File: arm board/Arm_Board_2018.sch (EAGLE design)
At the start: 190 parts, among them J1 RJ45KEYSTONE-942, J10 APP_2POS_CONFIGGENERAL_CONFIG, J11 APP_2POS_CONFIGGENERAL_CONFIG, J12 APP_2POS_CONFIGGENERAL_CONFIG, J13 APP_2POS_CONFIGGENERAL_CONFIG, J14 SL02, J15 SL02, J16 SL02, J2 JTAG_ARM_10PIN, J4 SL02, J5 APP_2POS_CONFIGGENERAL_CONFIG, J6 APP_2POS_CONFIGGENERAL_CONFIG, J7 APP_2POS_CONFIGGENERAL_CONFIG, J9 APP_2POS_CONFIGGENERAL_CONFIG, Q1 Q_IRF7437SMD, U1 TM4C1294NCPDT, U2 HX1198FNL, U3 SLVU2.8-4, Y1 NX3225GA, Y2 CRYATL_32K_SMD

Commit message: Switched wires to nets, corrected couple of naming errors
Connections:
- removed net MOTOR23_CURRENT_SENSOR: U$21.VOUT
- removed net N$52: C44.1, C45.1, C46.1, C47.1
- removed net N$82: R61.1, R62.1, R63.1, R64.1, R65.1, R66.1
- removed net N$85: R55.2
- removed net N$86: R54.2
- net GND: now also C44.1, C45.1, C46.1, C47.1, R54.2, R55.2, R61.1, R62.1, R63.1, R64.1, R65.1, R66.1
- net MOTOR3_CURRENT_SENSOR: now also U$21.VOUT
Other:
- note added: "MAIN POWER INPUT"
- note added: "MOTOR MANUAL CONTROL LEDS"
- note removed: "BOARD LEDS"
- note removed: "MAIN POWER LINE"
- moved on the sheet: C21, C23, C25, C26, C29, C30, C33, C34, C37, C38, C41, C42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

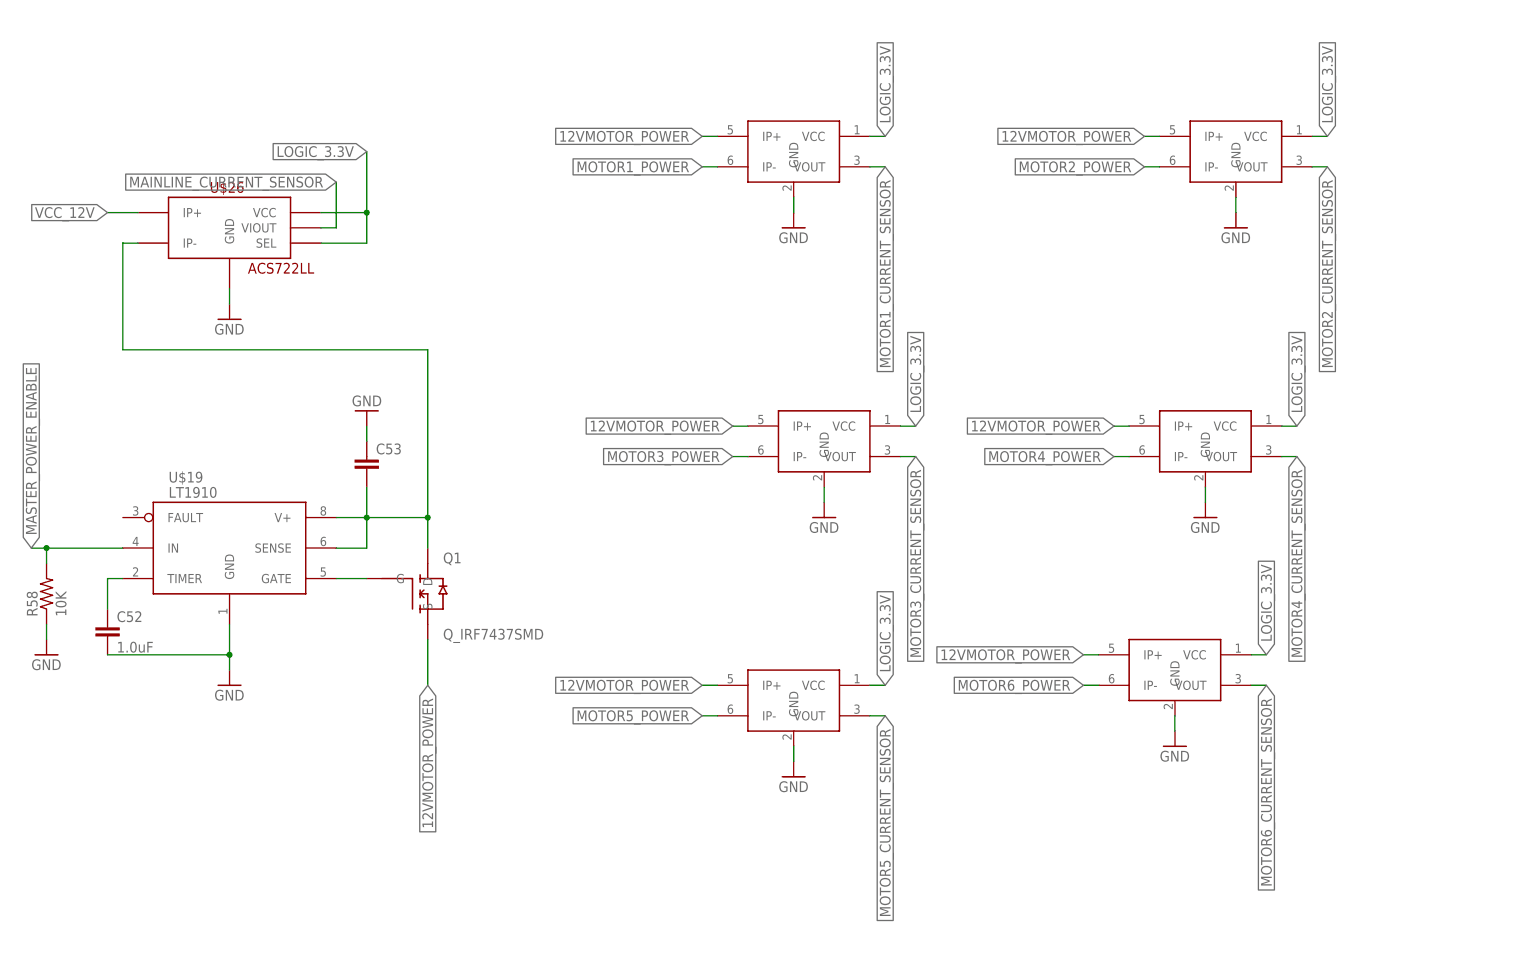
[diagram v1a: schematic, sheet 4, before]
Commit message: Fixed remaining SCH issues, warnings, and missing parts
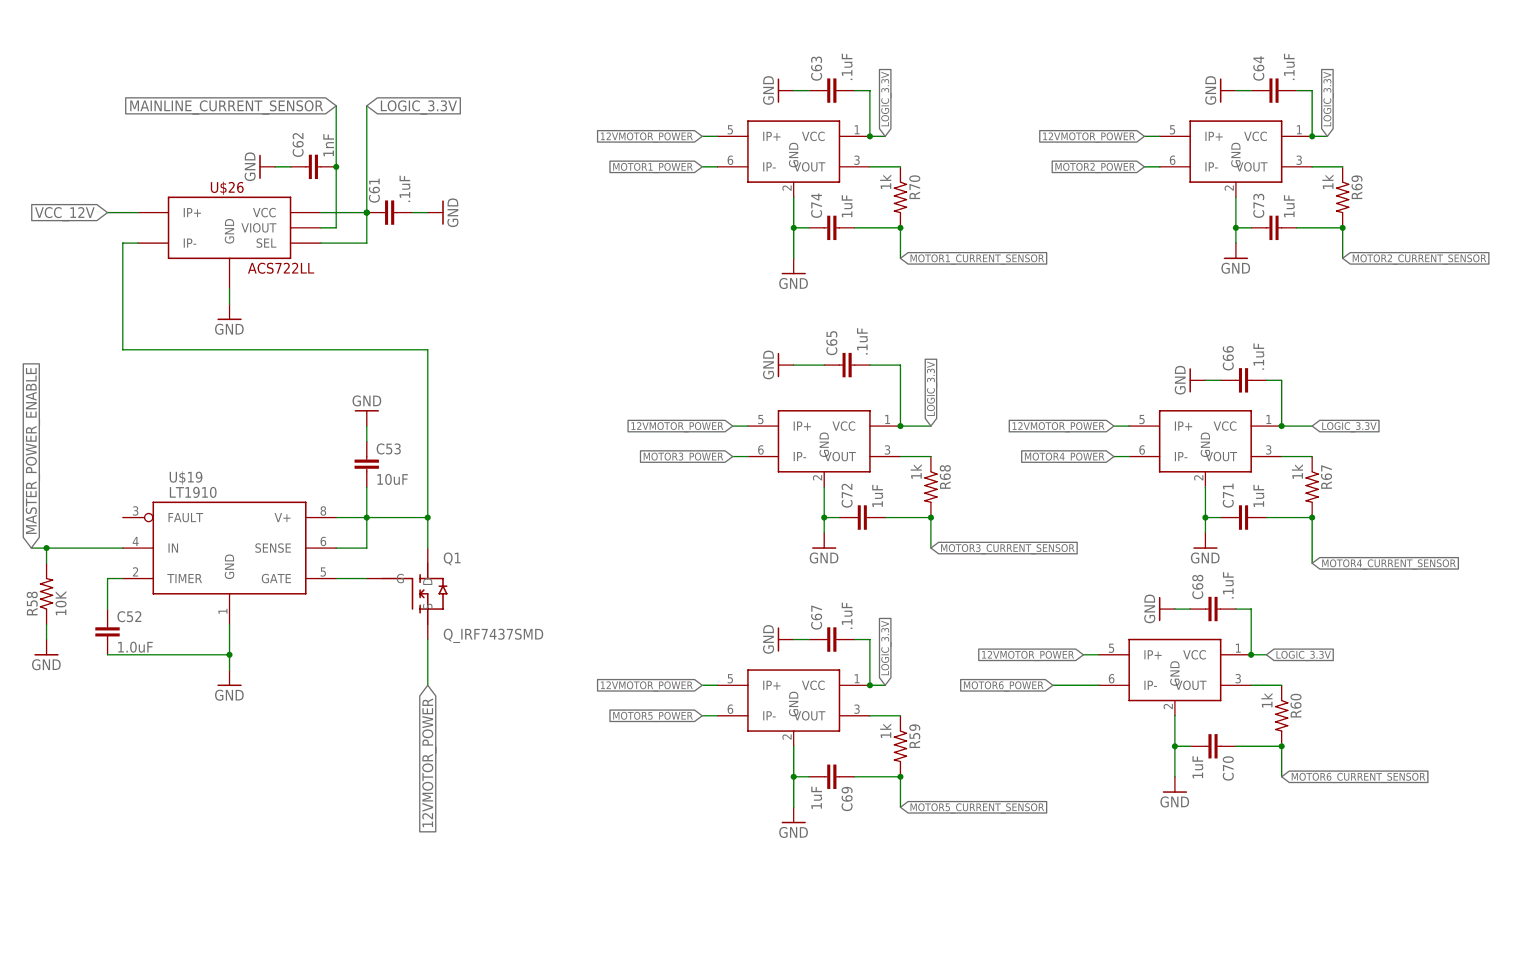
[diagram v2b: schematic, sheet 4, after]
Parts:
- removed C50: 2.2uF, SparkFun-Passives:CAP0603-CAP
- added C61, C63, C64, C65, C66, C67, C68: .1uF, SparkFun-Passives:CAP0603-CAP
- added C62: 1nF, SparkFun-Passives:CAP0603-CAP
- added C69, C70, C71, C72, C73, C74: 1uF, SparkFun-Passives:CAP0603-CAP
- added C75: 2.2uF, SparkFun-Capacitors:CAP1206
- added R59, R60, R67, R68, R69, R70: 1k, SparkFun-Passives:RESISTOR0402-RES
- C48, C49, C54: value (none) -> .1uF
- C51: device SparkFun-Passives:CAP0603-CAP -> SparkFun-Capacitors:CAP1206
- C53: value (none) -> 10uF
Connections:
- new net N$12: R59.1, U$24.VOUT
- new net N$13: R60.1, U$25.VOUT
- new net N$20: R67.1, U$23.VOUT
- new net N$32: R68.1, U$21.VOUT
- new net N$38: R69.1, U$22.VOUT
- new net N$44: R70.1, U$20.VOUT
- net GND: now also C51.1, C61.2, C62.1, C63.1, C64.1, C65.1, C66.1, C67.1, C68.1, C69.2, C70.2, C71.1, C72.1, C73.1, C74.1, C75.2; no longer C50.2, C51.2
- net LOGIC_3.3V: now also C61.1, C63.2, C64.2, C65.2, C66.2, C67.2, C68.2, C75.1; no longer C50.1
- net MAINLINE_CURRENT_SENSOR: now also C62.2
- net MOTOR1_CURRENT_SENSOR: now also C74.2, R70.2; no longer U$20.VOUT
- net MOTOR2_CURRENT_SENSOR: now also C73.2, R69.2; no longer U$22.VOUT
- net MOTOR3_CURRENT_SENSOR: now also C72.2, R68.2; no longer U$21.VOUT
- net MOTOR4_CURRENT_SENSOR: now also C71.2, R67.2; no longer U$23.VOUT
- net MOTOR5_CURRENT_SENSOR: now also C69.1, R59.2; no longer U$24.VOUT
- net MOTOR6_CURRENT_SENSOR: now also C70.1, R60.2; no longer U$25.VOUT
- net VCC_12V: now also C51.2; no longer C51.1
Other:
- moved on the sheet: C51

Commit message: Changed +3V3 to LOGIC_3.3V
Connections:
- removed net +3V3: C1.1, C10.1, C11.1, C2.1, C3.1, C4.1, C8.1, C9.1, J2.VTARGET, LED3.A, R1.1, R12.2, R13.2, R17.1, R2.1, R3.1, R4.1, U1G$2.VDD@101, U1G$2.VDD@113, U1G$2.VDD@122, U1G$2.VDD@16, U1G$2.VDD@26, U1G$2.VDD@28, U1G$2.VDD@39, U1G$2.VDD@47, U1G$2.VDD@51, U1G$2.VDD@52, U1G$2.VDD@69, U1G$2.VDD@7, U1G$2.VDD@79, U1G$2.VDD@90, U1G$2.VDDA@8, U1G$2.VREFA+@9, U2.P$2, U2.P$7
- net LOGIC_3.3V: now also C1.1, C10.1, C11.1, C2.1, C3.1, C4.1, C8.1, C9.1, J2.VTARGET, LED3.A, R1.1, R12.2, R13.2, R17.1, R2.1, R3.1, R4.1, U1G$2.VDD@101, U1G$2.VDD@113, U1G$2.VDD@122, U1G$2.VDD@16, U1G$2.VDD@26, U1G$2.VDD@28, U1G$2.VDD@39, U1G$2.VDD@47, U1G$2.VDD@51, U1G$2.VDD@52, U1G$2.VDD@69, U1G$2.VDD@7, U1G$2.VDD@79, U1G$2.VDD@90, U1G$2.VDDA@8, U1G$2.VREFA+@9, U2.P$2, U2.P$7
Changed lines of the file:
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@@
 </segment>
 </net>
-<net name="+3V3" class="0">
+<net name="LOGIC_3.3V" class="0">
 <segment>
 <pinref part="+3V1" gate="G$1" pin="+3V3"/>

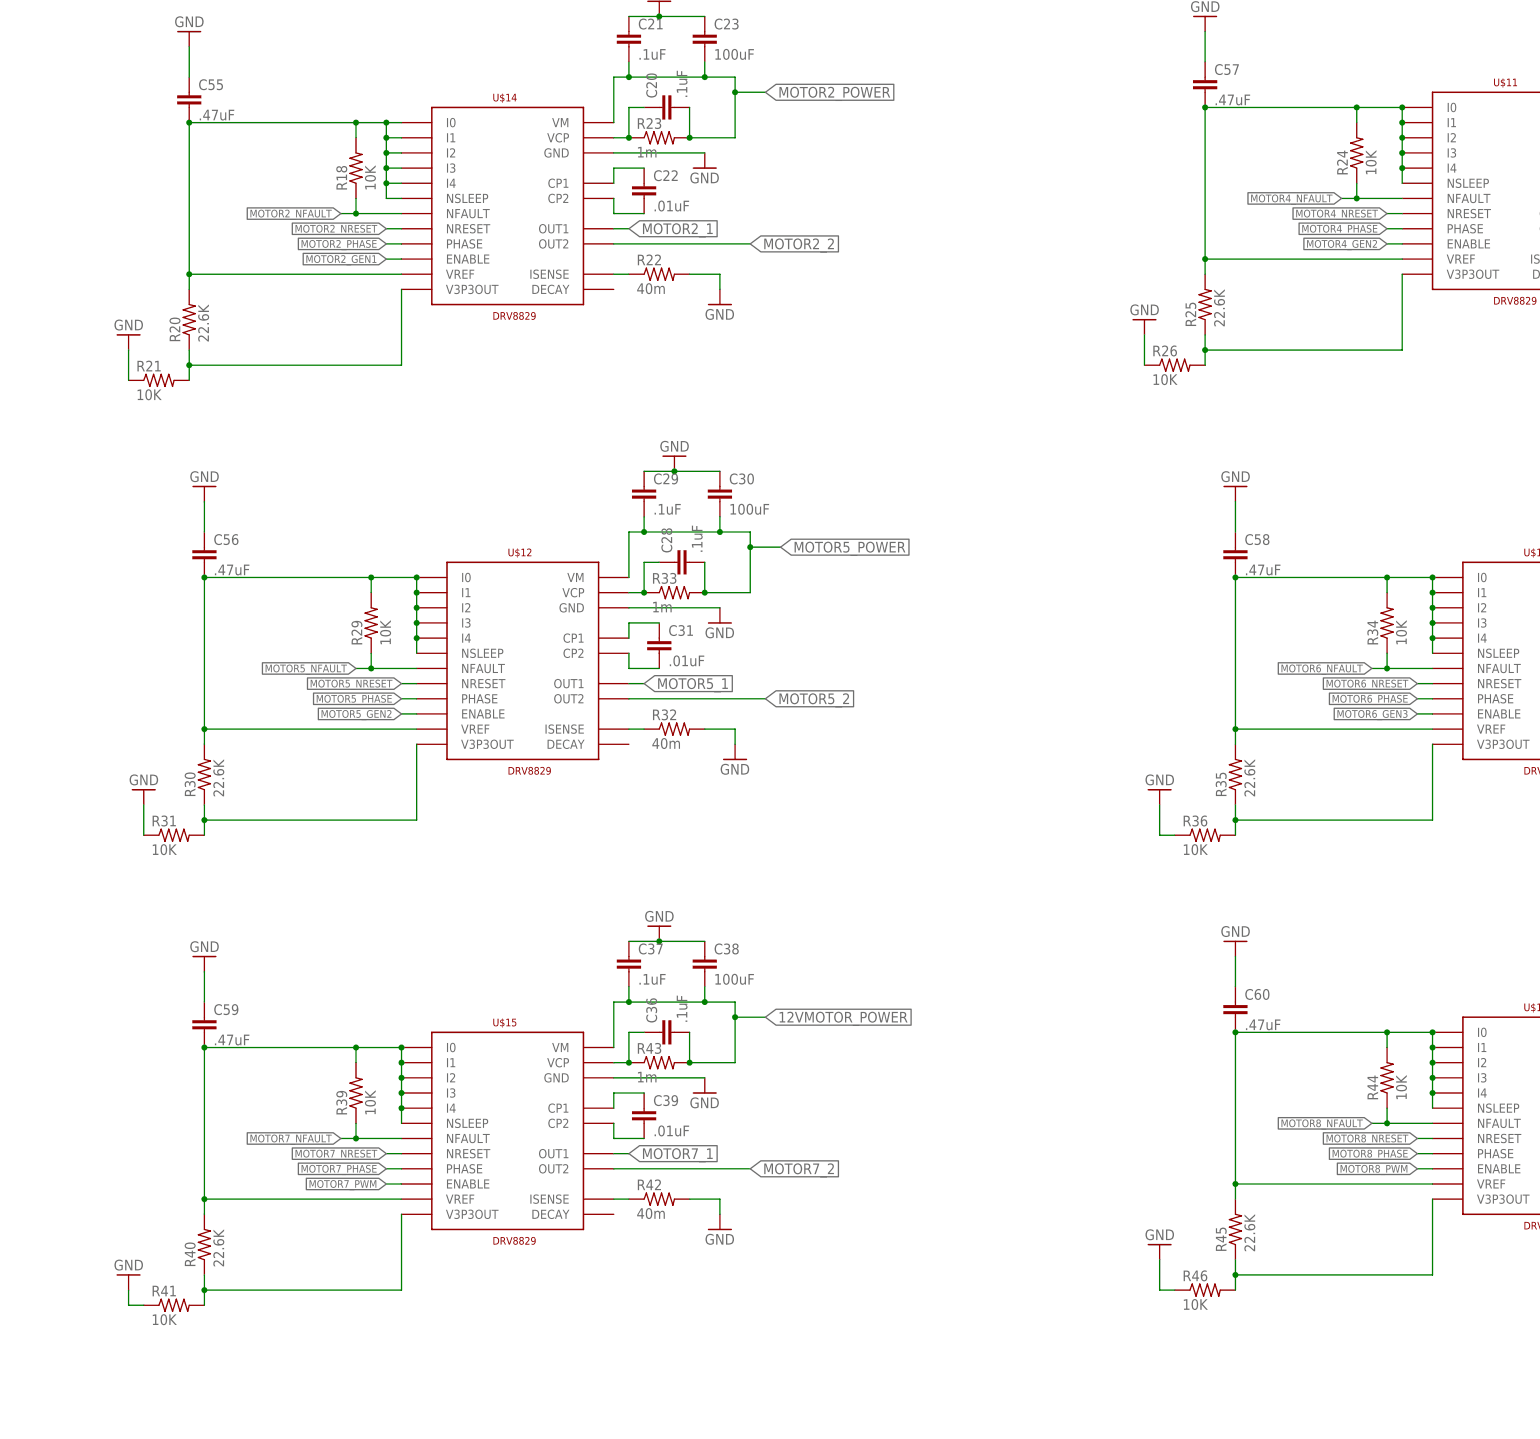
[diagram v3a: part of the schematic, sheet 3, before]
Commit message: Corrected error with resis div on H bridges
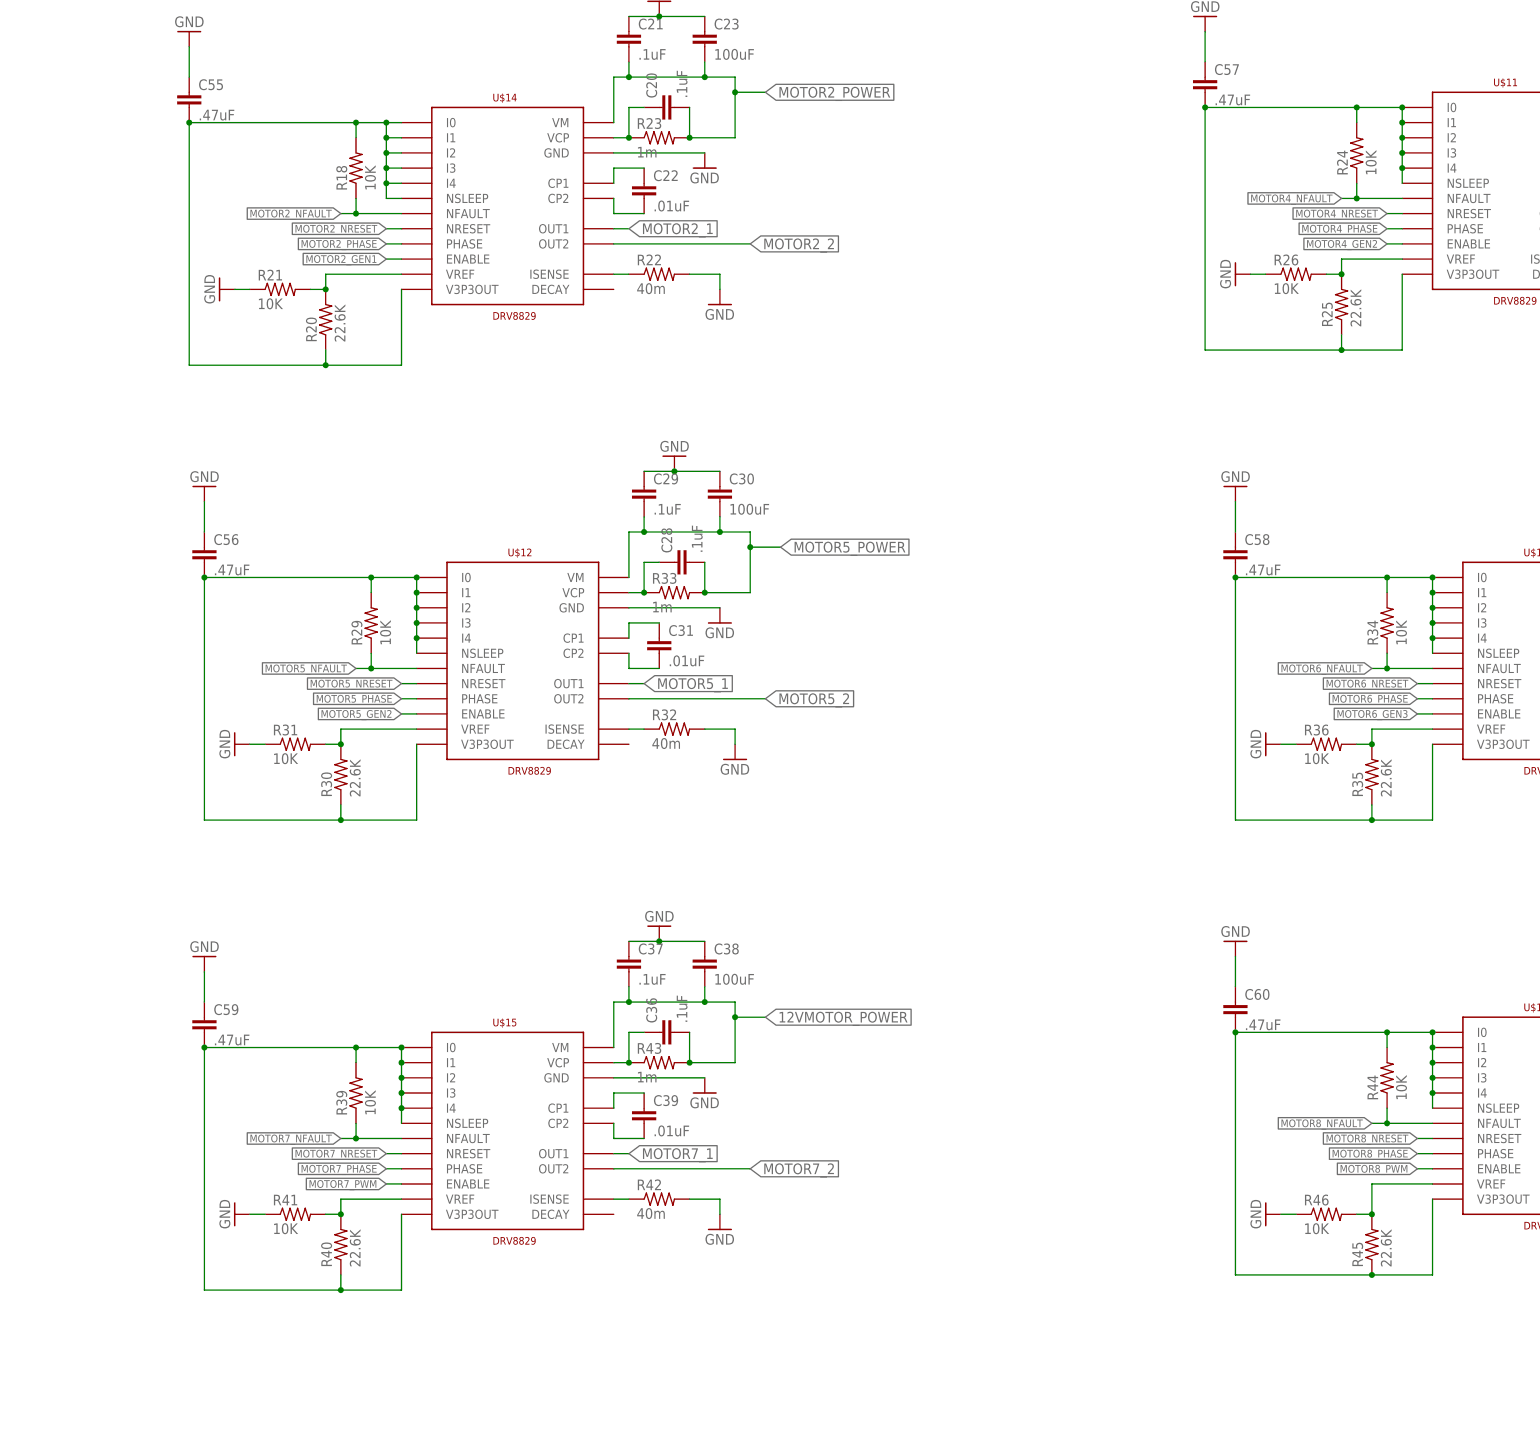
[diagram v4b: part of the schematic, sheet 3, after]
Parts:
- added C50: 2.2uF, SparkFun-Capacitors:CAP1206
- added GND97: APPPP45_PCB_HORIZ_RIGHT, MRDT-Connectors:APPPP45_PCB_HORIZ_RIGHT
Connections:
- net GND: now also C50.2
- net N$1: now also R26.2; no longer C57.2, R24.2, U$11.I0, U$11.I1, U$11.I2, U$11.I3, U$11.I4, U$11.NSLEEP
- net N$15: now also C57.2, R24.2, U$11.I0, U$11.I1, U$11.I2, U$11.I3, U$11.I4, U$11.NSLEEP; no longer R26.2
- net N$2: now also R31.2; no longer C56.2, R29.2, U$12.I0, U$12.I1, U$12.I2, U$12.I3, U$12.I4, U$12.NSLEEP
- net N$21: now also C56.2, R29.2, U$12.I0, U$12.I1, U$12.I2, U$12.I3, U$12.I4, U$12.NSLEEP; no longer R31.2
- net N$26: now also R36.2; no longer C58.2, R34.2, U$13.I0, U$13.I1, U$13.I2, U$13.I3, U$13.I4, U$13.NSLEEP
- net N$27: now also C58.2, R34.2, U$13.I0, U$13.I1, U$13.I2, U$13.I3, U$13.I4, U$13.NSLEEP; no longer R36.2
- net N$3: now also R20.1, U$14.V3P3OUT; no longer R20.2, U$14.VREF
- net N$33: now also C59.2, R39.2, U$15.I0, U$15.I1, U$15.I2, U$15.I3, U$15.I4, U$15.NSLEEP; no longer R41.2
- net N$39: now also C60.2, R44.2, U$16.I0, U$16.I1, U$16.I2, U$16.I3, U$16.I4, U$16.NSLEEP; no longer R46.2
- net N$4: now also R41.2; no longer C59.2, R39.2, U$15.I0, U$15.I1, U$15.I2, U$15.I3, U$15.I4, U$15.NSLEEP
- net N$5: now also R46.2; no longer C60.2, R44.2, U$16.I0, U$16.I1, U$16.I2, U$16.I3, U$16.I4, U$16.NSLEEP
- net N$6: now also R20.2, U$14.VREF; no longer R20.1, U$14.V3P3OUT
- net VCC_12V: now also C50.1, GND97.P$1
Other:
- moved on the sheet: C51, GND, R20, R21, R25, R26, R30, R31, R35, R36, R40, R41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

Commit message: Revert "Changed +3V3 to LOGIC_3.3V"
This reverts commit afd64b7472180079d62c8d462dc00da2640ede11.
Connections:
- new net +3V3: C1.1, C10.1, C11.1, C2.1, C3.1, C4.1, C8.1, C9.1, J2.VTARGET, LED3.A, R1.1, R12.2, R13.2, R17.1, R2.1, R3.1, R4.1, U1G$2.VDD@101, U1G$2.VDD@113, U1G$2.VDD@122, U1G$2.VDD@16, U1G$2.VDD@26, U1G$2.VDD@28, U1G$2.VDD@39, U1G$2.VDD@47, U1G$2.VDD@51, U1G$2.VDD@52, U1G$2.VDD@69, U1G$2.VDD@7, U1G$2.VDD@79, U1G$2.VDD@90, U1G$2.VDDA@8, U1G$2.VREFA+@9, U2.P$2, U2.P$7
- net LOGIC_3.3V: no longer C1.1, C10.1, C11.1, C2.1, C3.1, C4.1, C8.1, C9.1, J2.VTARGET, LED3.A, R1.1, R12.2, R13.2, R17.1, R2.1, R3.1, R4.1, U1G$2.VDD@101, U1G$2.VDD@113, U1G$2.VDD@122, U1G$2.VDD@16, U1G$2.VDD@26, U1G$2.VDD@28, U1G$2.VDD@39, U1G$2.VDD@47, U1G$2.VDD@51, U1G$2.VDD@52, U1G$2.VDD@69, U1G$2.VDD@7, U1G$2.VDD@79, U1G$2.VDD@90, U1G$2.VDDA@8, U1G$2.VREFA+@9, U2.P$2, U2.P$7
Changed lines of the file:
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@@
 </segment>
 </net>
-<net name="LOGIC_3.3V" class="0">
+<net name="+3V3" class="0">
 <segment>
 <pinref part="+3V1" gate="G$1" pin="+3V3"/>
